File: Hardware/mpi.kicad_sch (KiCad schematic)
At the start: 22 parts, among them J5 J-0530471010, J8 J-0532610471, U10 MAX3086EESD+T, U9 U-MAX3378EEUD+T

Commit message: Connect connectors
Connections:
- net 5V renamed +5V

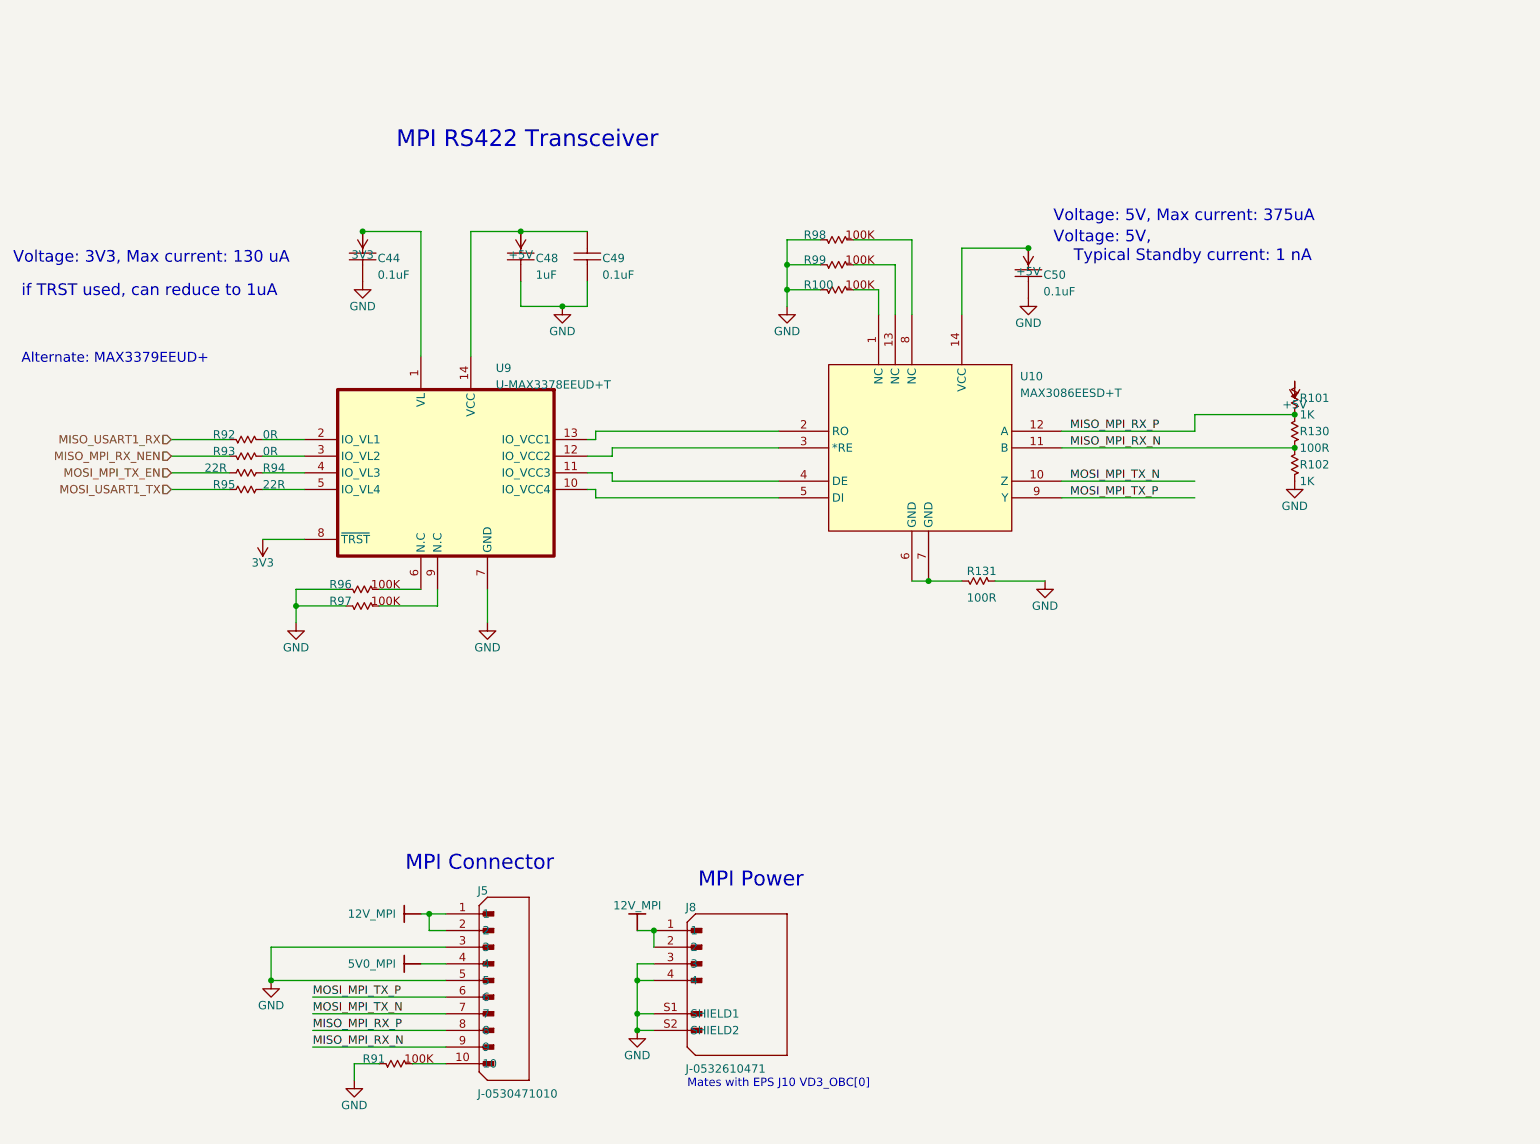
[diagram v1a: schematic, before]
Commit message: Add STM32 Reset Switch & RP2040 I2C pins
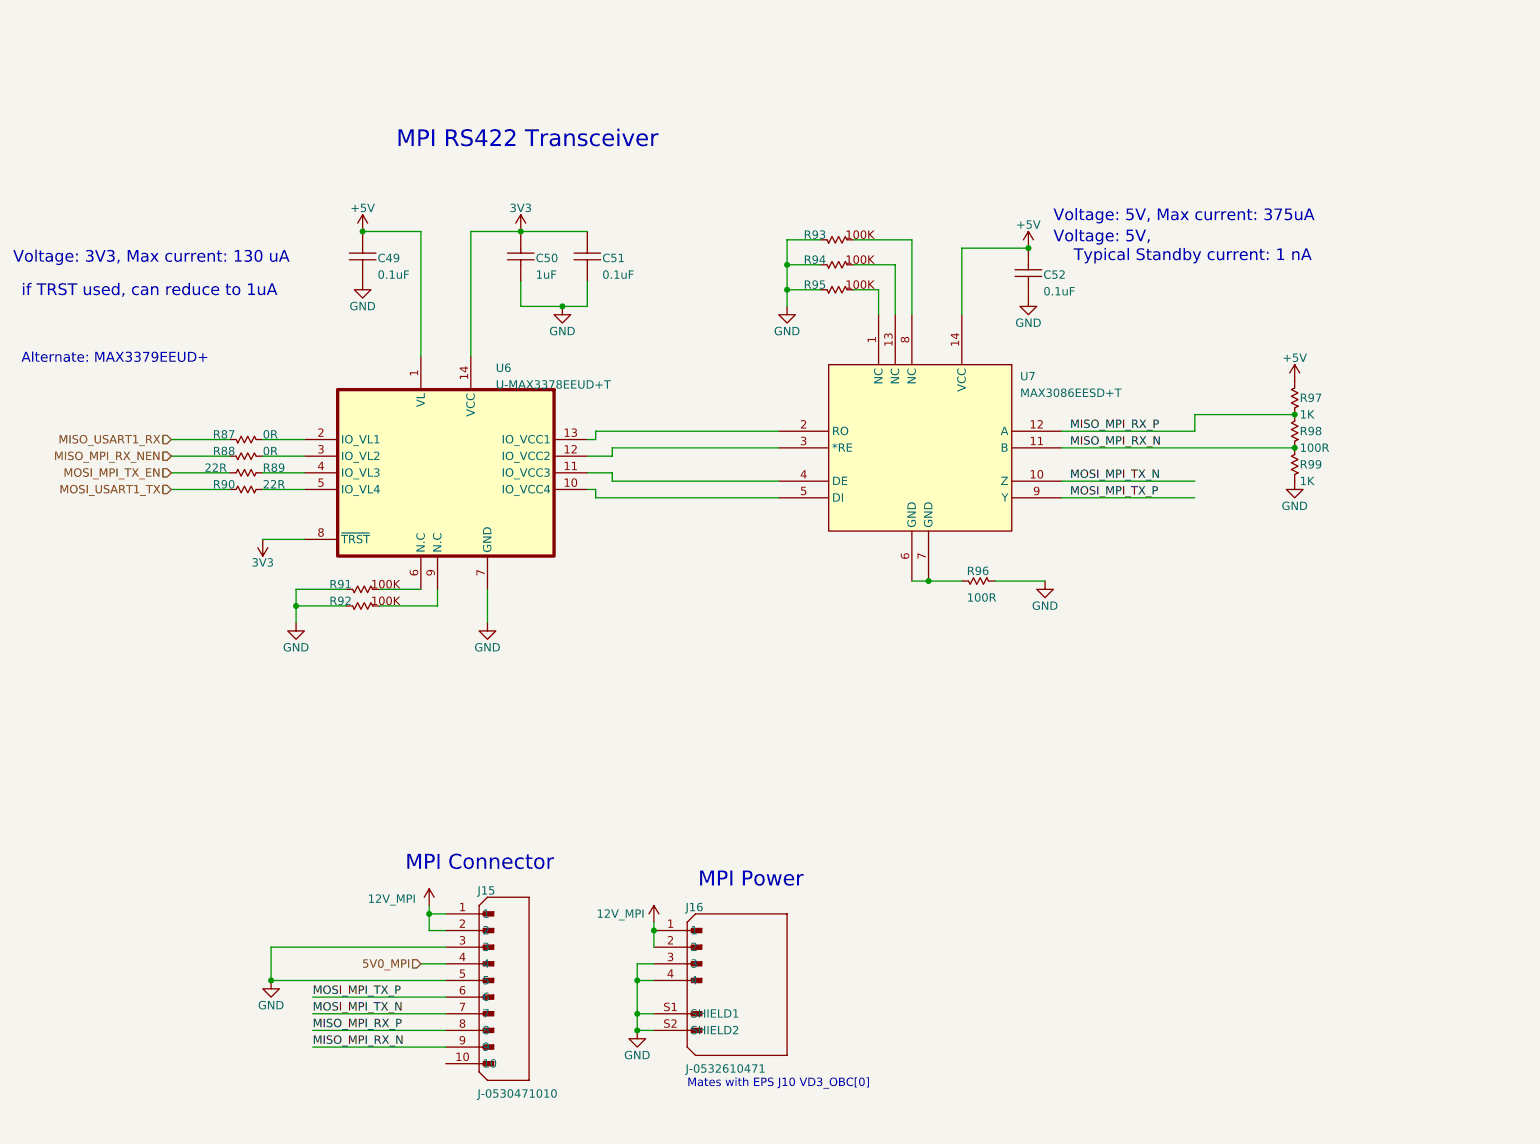
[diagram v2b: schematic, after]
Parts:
- removed R91: 100K, 0603, symbol OBC Development Board:root_0_RT-100K0-F-1/16W-0603_OBC Development Board.SchLib
- renumbered C44 to C49, C48 to C50, C49 to C51, C50 to C52, J5 to J15, J8 to J16, R92 to R87, R93 to R88, R94 to R89, R95 to R90, R96 to R91, R97 to R92, R98 to R93, R99 to R94, R100 to R95, R131 to R96, R101 to R97, R130 to R98, R102 to R99, U9 to U6, U10 to U7
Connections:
- net +5V: now also C49.1, U6.1 (VL); no longer C50.2, C51.1, U6.14 (VCC)
- net 3V3: now also C50.2, C51.1, U6.14 (VCC); no longer C49.1, U6.1 (VL)

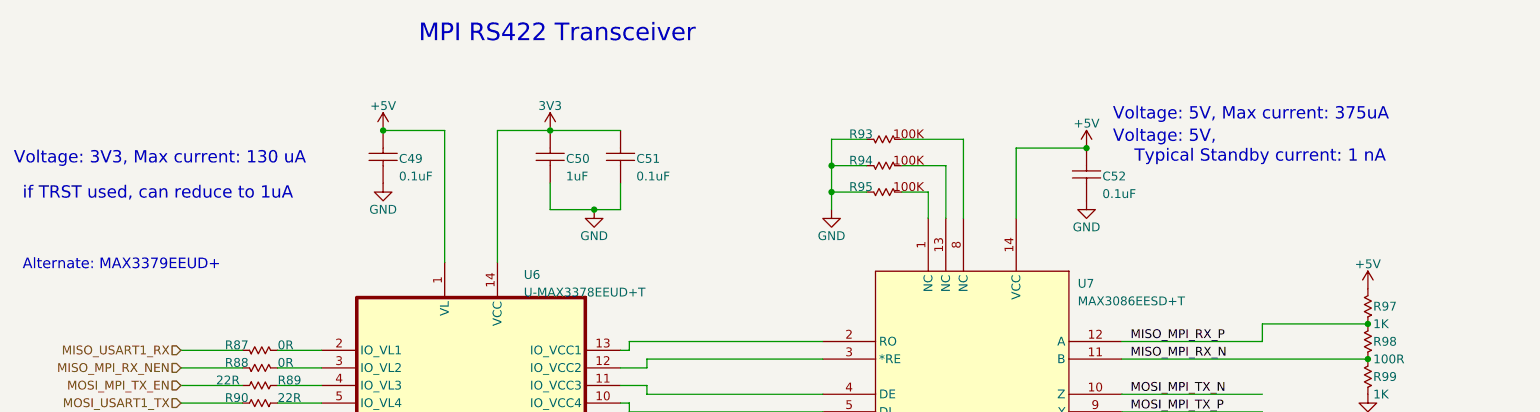
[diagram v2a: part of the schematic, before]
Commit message: Move ANT to RP2040
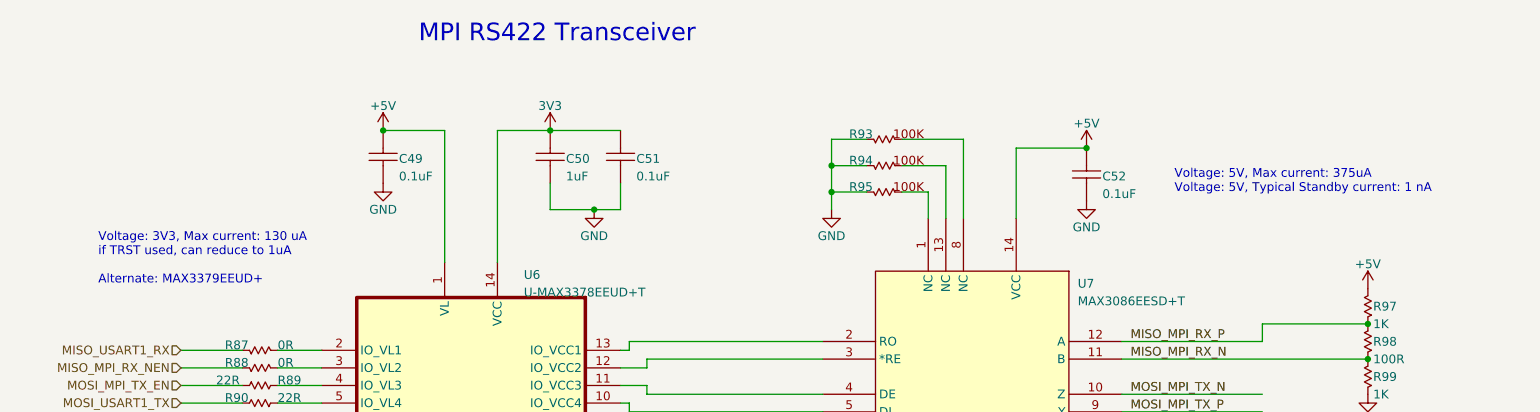
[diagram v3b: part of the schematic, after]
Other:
- note added: "Voltage: 3V3, Max current: 130 uA if TRST used, can reduce to 1uA Alternate: MAX3379EEUD+"
- note added: "Voltage: 5V, Max current: 375uA Voltage: 5V, Typical Standby current: 1 nA"
- note removed: "Alternate: MAX3379EEUD+"
- note removed: "Voltage: 3V3, Max current: 130 uA"
- note removed: "Voltage: 5V, Max current: 375uA"
- note removed: "Voltage: 5V, Typical Standby current: 1 nA"
- note removed: "if TRST used, can reduce to 1uA"
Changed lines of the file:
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@@
 	(generator_version "9.0")
 	(paper "A3")
-	(text "Alternate: MAX3379EEUD+"
+	(text "Voltage: 3V3, Max current: 130 uA\nif TRST used, can reduce to 1uA\n\nAlternate: MAX3379EEUD+"
 		(exclude_from_sim no)
-		(at 44.45 72.39 0)
+		(at 55.372 74.422 0)
 		(effects
 			(font
-				(size 1.524 1.524)
+				(size 1.27 1.27)
+			)
+			(justify left bottom)
+		)
+	)
+	(text "Voltage: 5V, Max current: 375uA\nVoltage: 5V, Typical Standby current: 1 nA"
+		(exclude_from_sim no)
+		(at 210.82 61.214 0)
+		(effects
+			(font
+				(size 1.27 1.27)
 			)
 			(justify left bottom)
@@
 		)
 	)
-	(text "Voltage: 5V, Max current: 375uA"
-		(exclude_from_sim no)
-		(at 201.93 50.8 0)
-		(effects
-			(font
-				(size 1.778 1.778)
-			)
-			(justify left bottom)
-		)
-	)
 	(text "MPI Connector"
 		(exclude_from_sim no)
@@
 		)
 	)
-	(text "if TRST used, can reduce to 1uA"
-		(exclude_from_sim no)
-		(at 44.45 62.23 0)
-		(effects
-			(font
-				(size 1.778 1.778)
-			)
-			(justify left bottom)
-		)
-	)
-	(text "Voltage: 5V, \n	Typical Standby current: 1 nA"
-		(exclude_from_sim no)
-		(at 201.93 56.896 0)
-		(effects
-			(font
-				(size 1.778 1.778)
-			)
-			(justify left bottom)
-		)
-	)
-	(text "Voltage: 3V3, Max current: 130 uA"
-		(exclude_from_sim no)
-		(at 43.18 57.15 0)
-		(effects
-			(font
-				(size 1.778 1.778)
-			)
-			(justify left bottom)
-		)
-	)

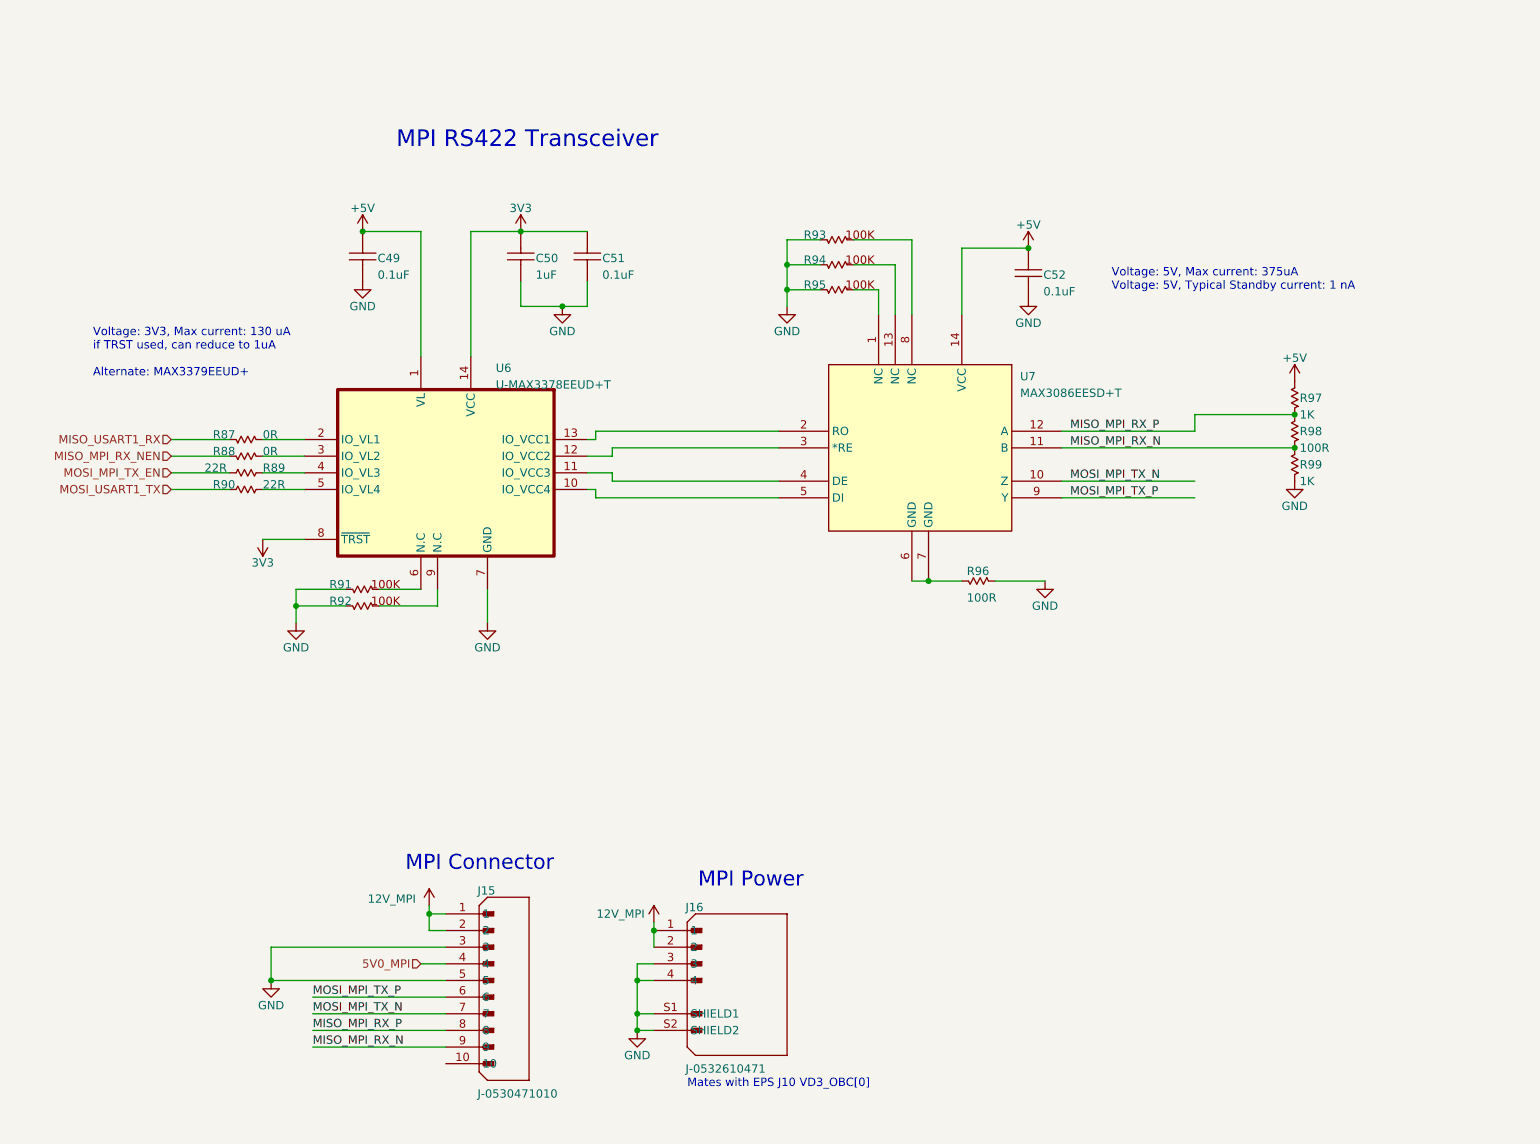
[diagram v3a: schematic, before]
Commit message: Add RP2040 SWD
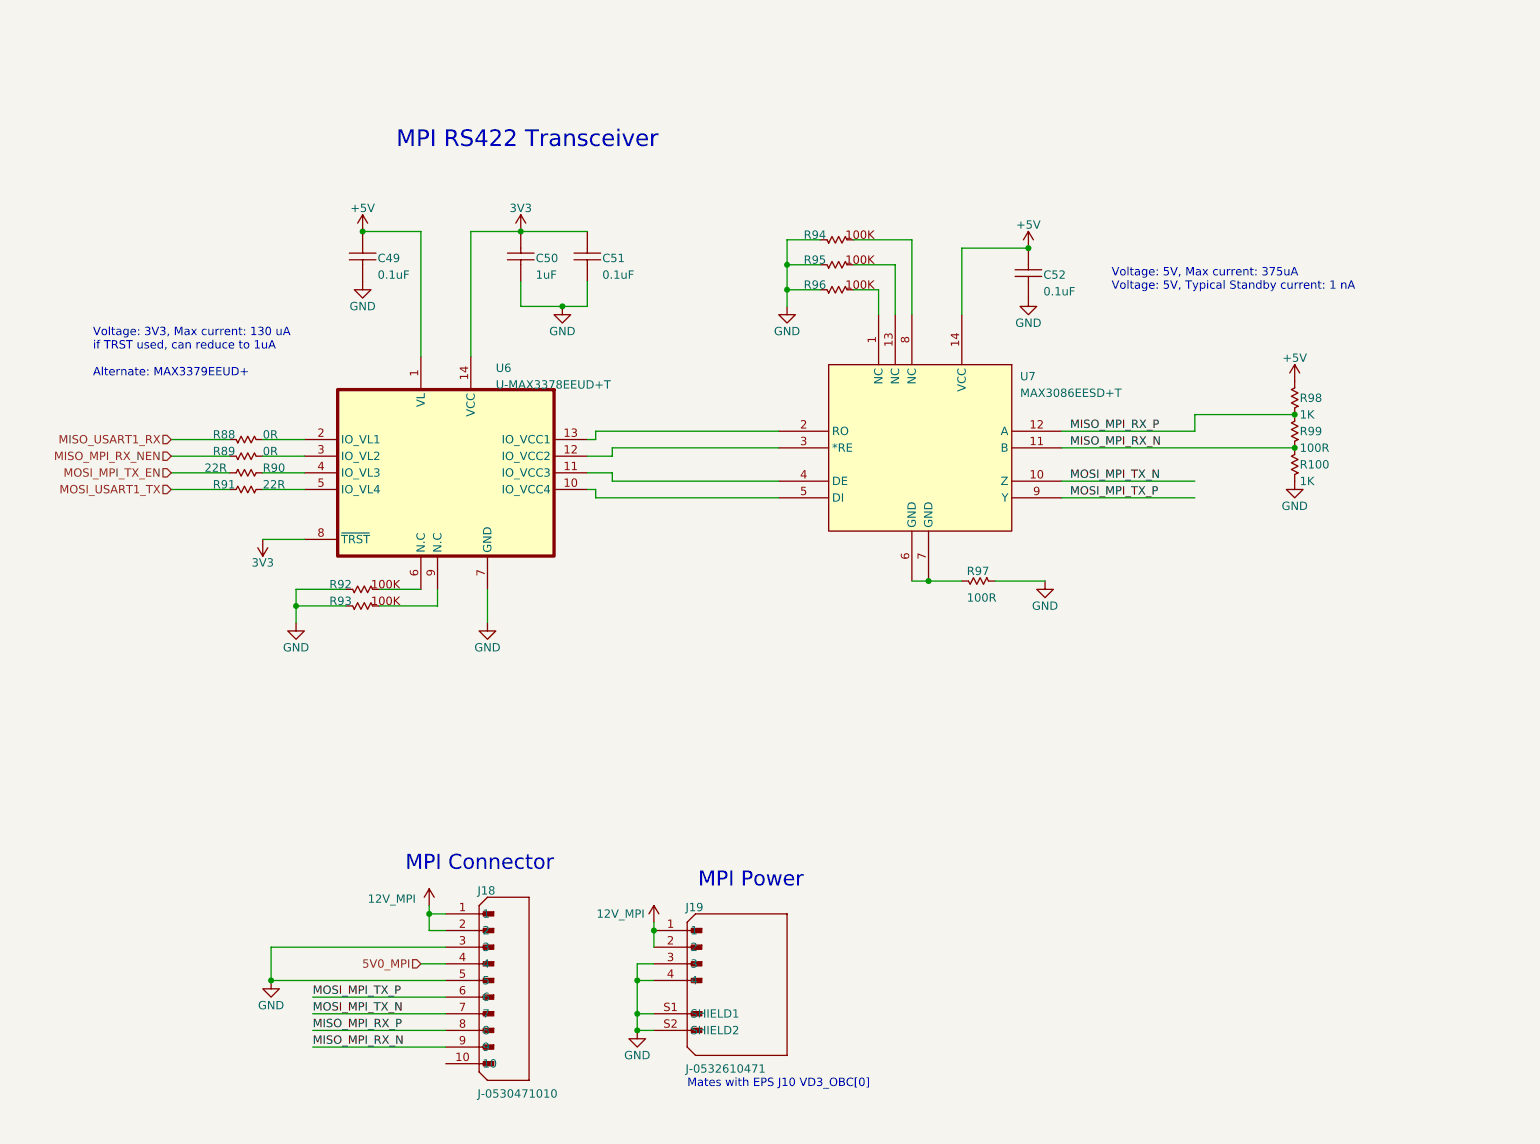
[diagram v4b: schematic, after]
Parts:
- renumbered J15 to J18, J16 to J19, R99 to R100, R87 to R88, R88 to R89, R89 to R90, R90 to R91, R91 to R92, R92 to R93, R93 to R94, R94 to R95, R95 to R96, R96 to R97, R97 to R98, R98 to R99

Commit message: Finish schematic v1
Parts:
- renumbered J18 to J22, J19 to J23, R88 to R87, R89 to R88, R90 to R89, R91 to R90, R92 to R91, R93 to R92, R94 to R93, R95 to R94, R96 to R95, R97 to R96, R98 to R97, R99 to R98, R100 to R99
